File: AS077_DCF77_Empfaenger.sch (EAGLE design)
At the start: 82 parts, among them IC1 CA3130E, IC2 4093N, IC3 4538N, IC4 4093N, J1 Rückkopplung, J2 JUMPER_J5MM, J3 JUMPER_J5MM, Q1 34MM_PIEZO, T1 BC549C, T2 BF244A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

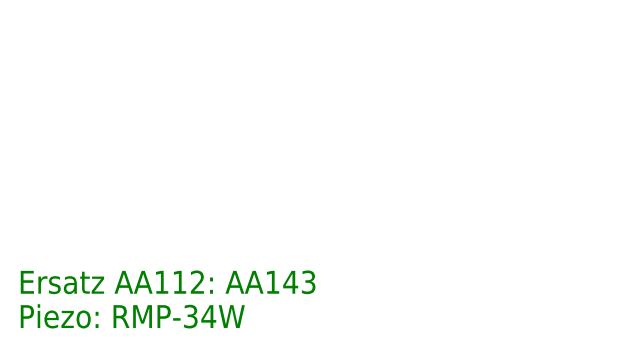
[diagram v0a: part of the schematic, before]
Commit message: updated LBR and BRD: Solder pin holes are now 1.4mm drills instead of 1.3
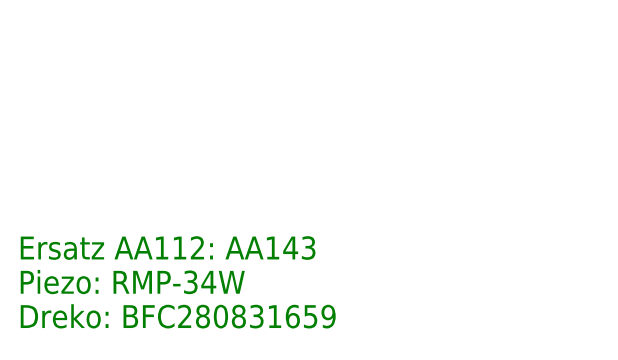
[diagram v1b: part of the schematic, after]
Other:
- note added: "Ersatz AA112: AA143 Piezo: RMP-34W Dreko: BFC280831659"
- note removed: "Ersatz AA112: AA143 Piezo: RMP-34W"
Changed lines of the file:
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@@
 <setting verticaltext="up"/>
 </settings>
-<grid distance="0.1" unitdist="inch" unit="inch" style="lines" multiple="1" display="yes" altdistance="0.01" altunitdist="inch" altunit="inch"/>
+<grid distance="0.1" unitdist="inch" unit="inch" style="lines" multiple="1" display="no" altdistance="0.01" altunitdist="inch" altunit="inch"/>
 <layers>
 <layer number="1" name="Top" color="4" fill="1" visible="no" active="no"/>
@@
 <text x="231.14" y="228.6" size="1.778" layer="97">Drahtbrücke bei 5V</text>
 <text x="7.62" y="7.62" size="2.54" layer="91">Ersatz AA112: AA143
-Piezo: RMP-34W</text>
+Piezo: RMP-34W
+Dreko: BFC280831659</text>
 <text x="154.94" y="116.84" size="2.54" layer="91" align="center">x</text>
 <text x="218.44" y="218.44" size="2.54" layer="91" align="center">x</text>
